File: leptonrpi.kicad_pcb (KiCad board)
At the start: 2 copper layers, 35 x 65 mm, 19 parts, among them J1 Raspberry_Pi_2_3, Q1 BSS84, Q2 BSS84, U1 TLV73312PDBV, U2 TLV73328PDBV, U3 TLV73328PDBV, U4 ASDMB-xxxMHz, U5 TXB0104D, U6 PCA9306D_118, U7 Flir_LEPTON

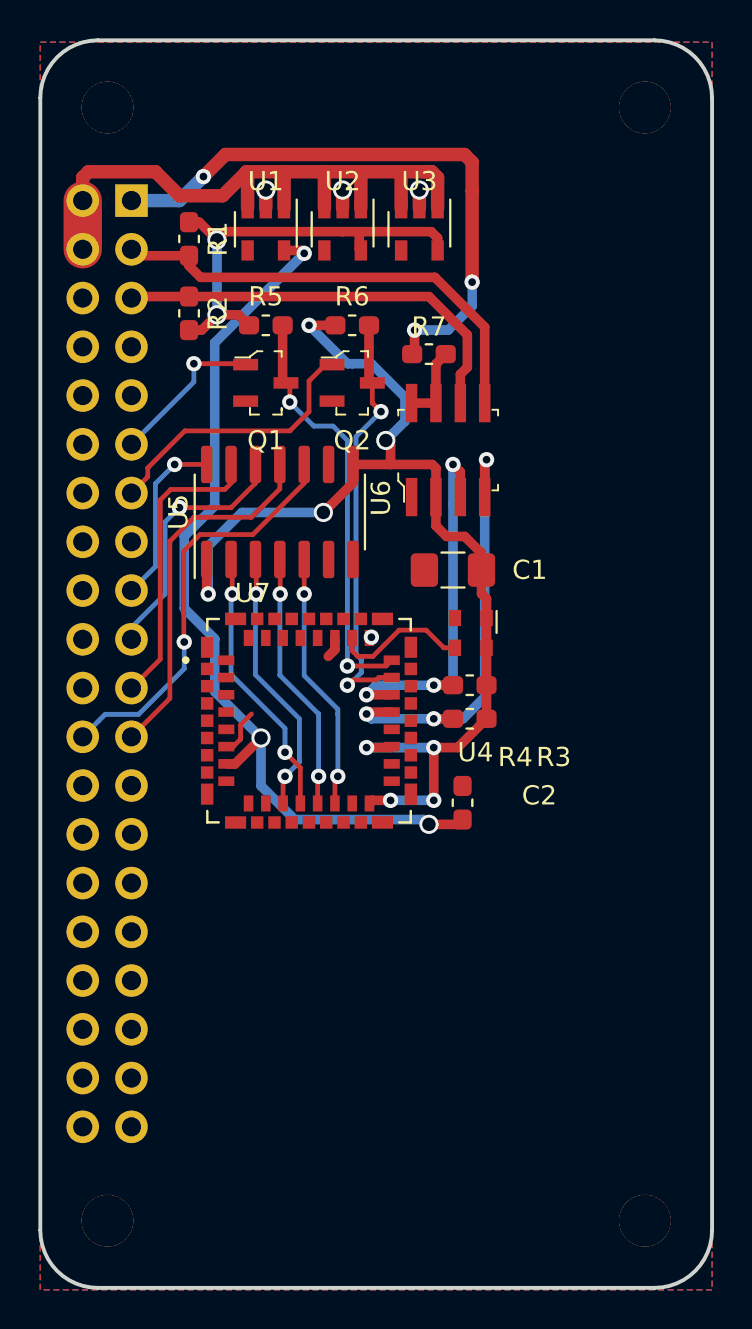
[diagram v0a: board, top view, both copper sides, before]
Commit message: rev a
removed all the vias that were in pads
added labels
added fun
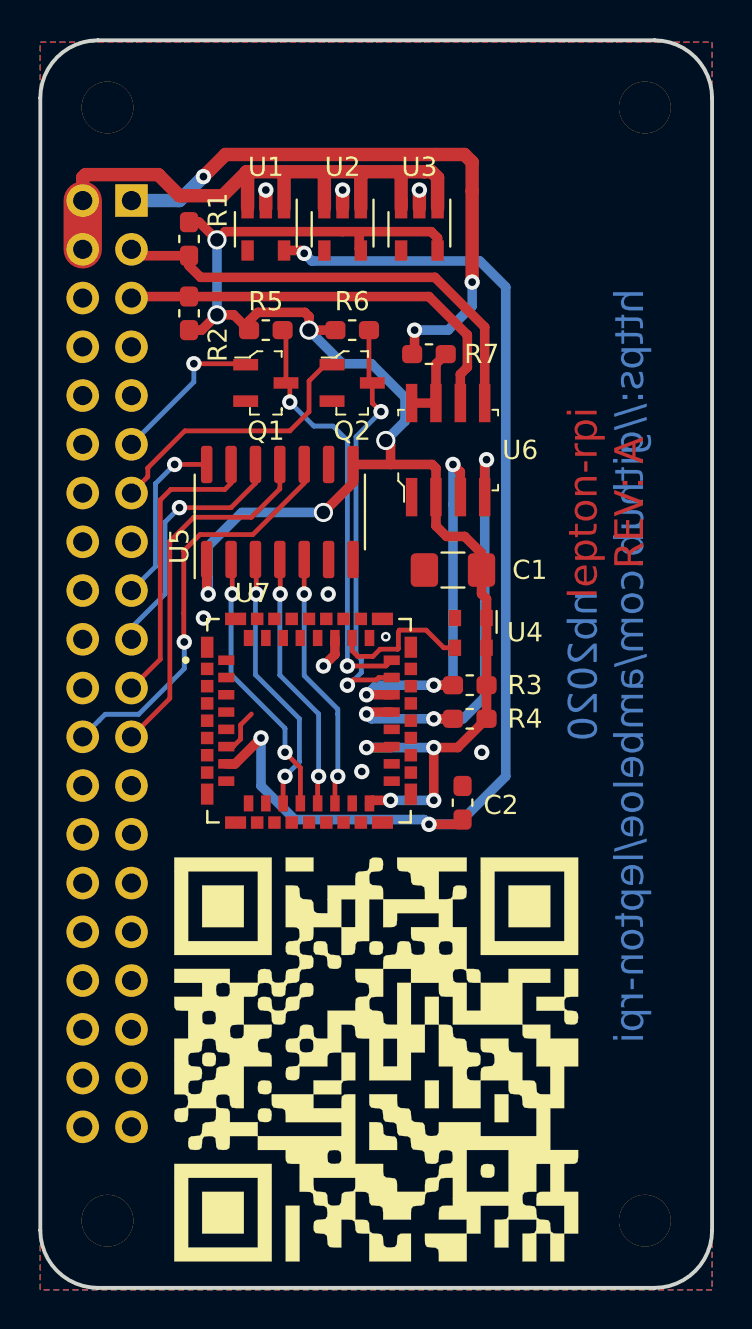
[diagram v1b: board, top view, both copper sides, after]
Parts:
- added G***: LOGO, misc footprints:nevergonnagiveyouup, F.Cu at (142.5, 123.0)
- moved R5 0.25 mm to (136.8, 85.0)
- moved R6 0.25 mm to (141.2, 85.0)
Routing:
- net +1V2: track 46.9 -> 59.2 mm
- net +2V8: track 82.6 -> 87.1 mm
- net GND: track 6.52 -> 7.18 mm, vias 4 -> 9
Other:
- net class Default: clearance 0.2 -> 0.15
- net class chungus power: clearance 0.2 -> 0.15
- rule trace_clearance: 0.2 -> 0.15
- board text added: "lepton-rpi REV: A"
- board text added: "nb2020 https://github.com/ambeloe/lepton-rpi"

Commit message: REV: A final
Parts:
- U7: footprint misc footprints:MOLEX_105028-1001 -> digikey-footprints:FLIR_Lepton_Socket_1050281001
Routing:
- net GND: vias 9 -> 10
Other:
- board text added: "THIS SIDE MUST FACE THE BOTTOM OF THE PI"

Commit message: fixed width
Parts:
- removed G***: LOGO, misc footprints:nevergonnagiveyouup
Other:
- board size 35 x 65 mm -> 30 x 65 mm
- board text added: "https://github.com/ambeloe/lepton-rpi"
- board text added: "lepton-rpi REV: B"
- board text added: "nb2020"
- board text removed: "lepton-rpi REV: A"
- board text removed: "nb2020 https://github.com/ambeloe/lepton-rpi"

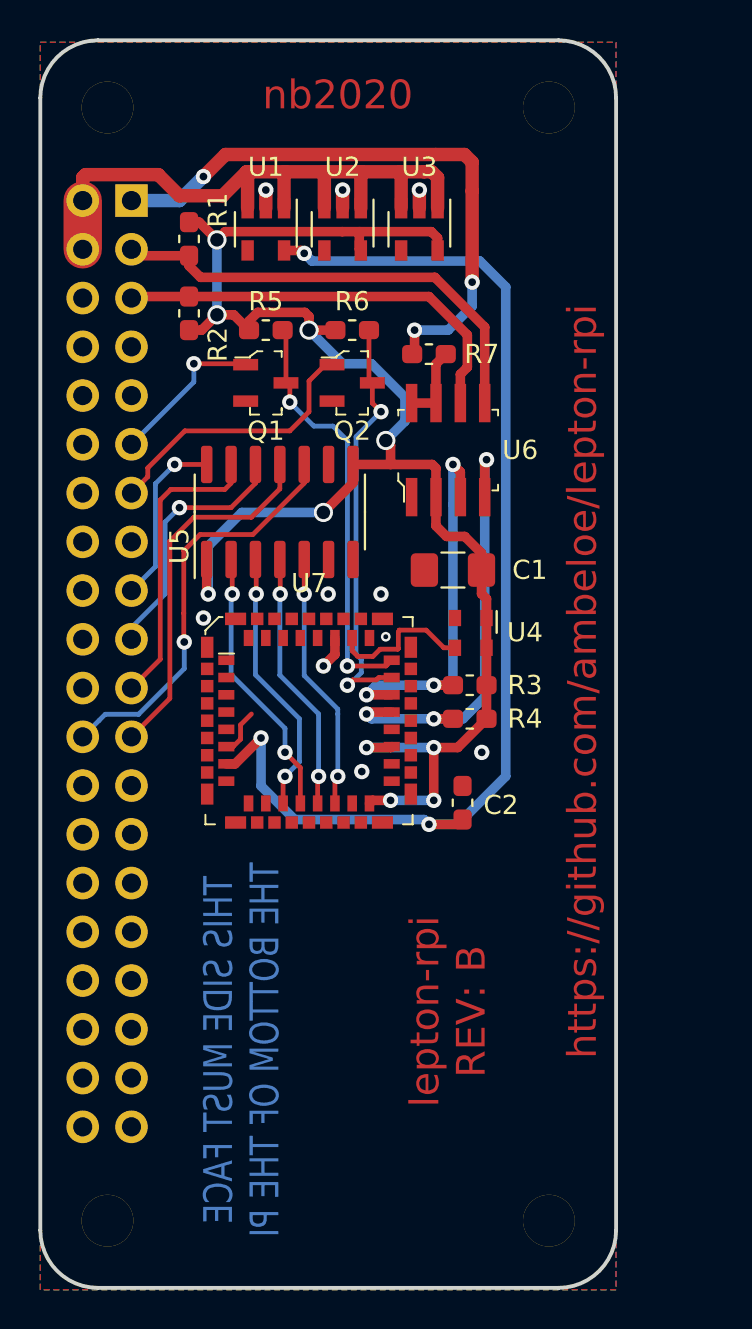
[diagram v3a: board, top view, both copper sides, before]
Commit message: should have fixed the i2c bus being reversed
rev c
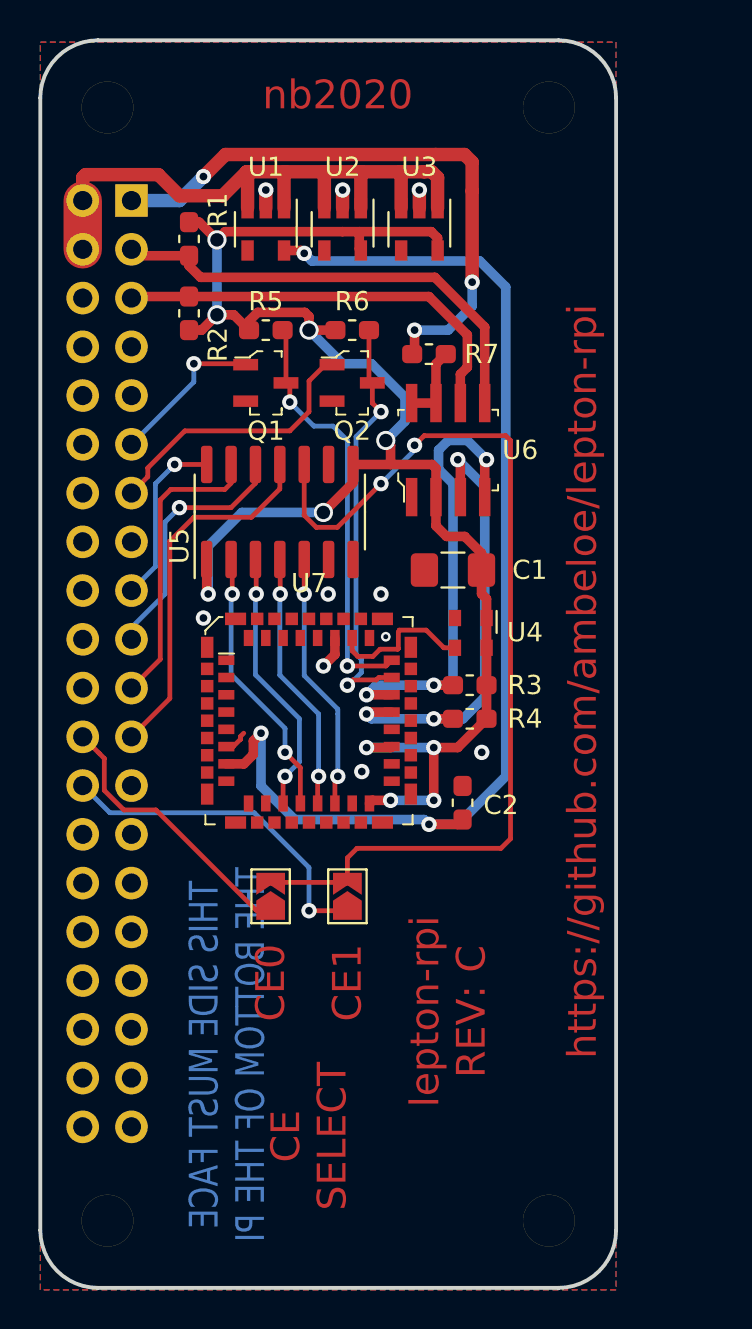
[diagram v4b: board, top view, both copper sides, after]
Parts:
- added JP1: SolderJumper_2_Open, Jumper:SolderJumper-2_P1.3mm_Open_TrianglePad1.0x1.5mm, F.Cu at (141.0, 114.5)
- added JP2: SolderJumper_2_Open, Jumper:SolderJumper-2_P1.3mm_Open_TrianglePad1.0x1.5mm, F.Cu at (137.0, 114.5)
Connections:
- net Net-(J1-Pad19) renamed /MOSI
- net Net-(J1-Pad21) renamed /MISO
- net Net-(U5-Pad2) renamed /L_MISO
- net Net-(U5-Pad3) renamed /L_MOSI
- net Net-(U5-Pad4) renamed /L_SCLK
- net Net-(U5-Pad5) renamed /L_CS
- J1 pad 23: Net-(J1-Pad23) -> CLK
- R1 pad 1: +2V8 -> +3V3
- R2 pad 1: +2V8 -> +3V3
- U5 pad 10: Net-(J1-Pad24) -> /CS
- U5 pad 11: Net-(J1-Pad23) -> CLK
- U6 pad 3: LSDA0 -> LSCL0
- U6 pad 4: LSCL0 -> LSDA0
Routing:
- net /CS: track 0.00 -> 50.8 mm, vias 0 -> 2
- net Net-(J1-Pad23): track 19.1 -> 0.00 mm
- net CLK: track 7.56 -> 26.7 mm
- net Net-(J1-Pad26): track 0.00 -> 17.8 mm, vias 0 -> 1
- net Net-(J1-Pad24): track 21.6 -> 14.5 mm, vias 1 -> 0
- net LSDA0: track 20.4 -> 24.9 mm
- net GND: track 7.18 -> 6.02 mm
- net +1V2: track 59.2 -> 59.7 mm
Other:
- board text added: "CE SELECT"
- board text added: "CE0"
- board text added: "CE1"
- board text added: "lepton-rpi REV: C"
- board text removed: "lepton-rpi REV: B"
